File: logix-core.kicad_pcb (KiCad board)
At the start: 6 copper layers, 82 parts, among them J1 QSH-030-01-X-D-A-XX, J2 QSH-030-01-X-D-A-XX, J3 878321420, U1 XC7A15T-CSG325, U2 MP5470GL-0000-P, U3 TPUSBLC6-4SC6, U4 FT230XQ, U5 MX25L3233FZN, U6 XC7A15T-CSG325, U8 MT41K256M16TW-107:P

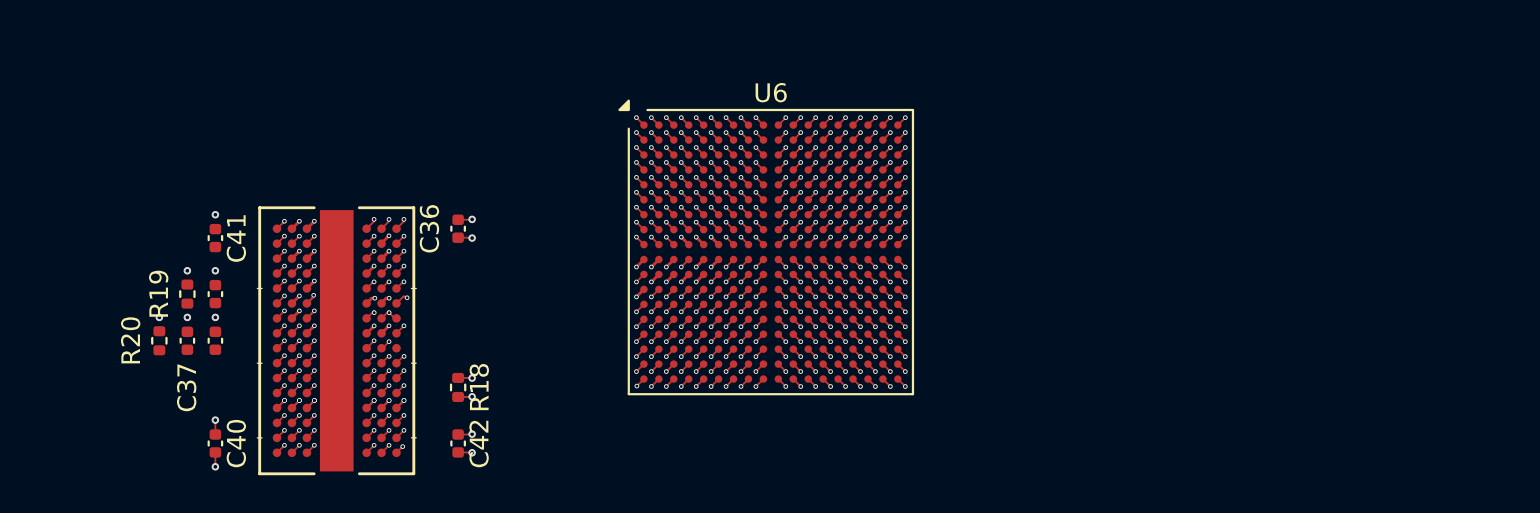
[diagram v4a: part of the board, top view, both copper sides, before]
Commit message: changed die to pad length for ddr3
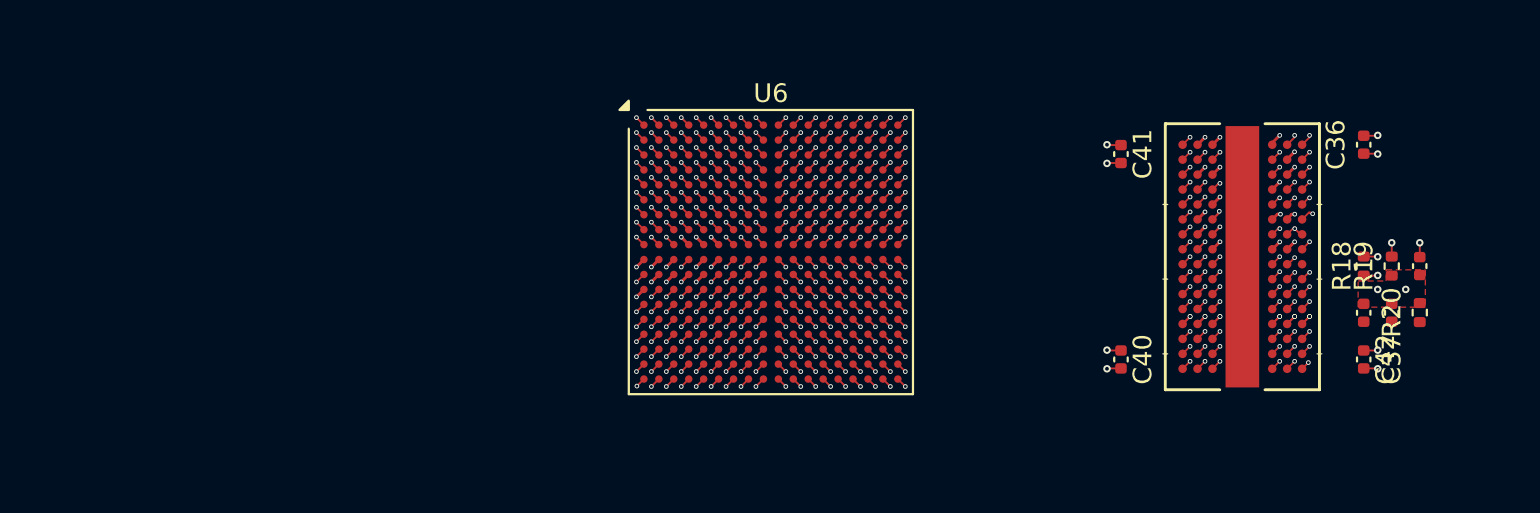
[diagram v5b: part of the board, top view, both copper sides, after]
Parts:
- moved R20 67.5 mm to (216.0, 146.0)
- moved C37 64.5 mm to (214.5, 146.0)
- moved C39 64.5 mm to (216.0, 143.5)
- moved R19 64.5 mm to (214.5, 143.5)
- moved C38 61.5 mm to (213.0, 146.0)
- moved R18 48.9 mm to (213.0, 143.5), turned to 90 degrees
- moved C36 48.7 mm to (213.0, 137.0)
- moved C40 48.7 mm to (200.0, 148.5)
- moved C41 48.7 mm to (200.0, 137.5)
- moved C42 48.7 mm to (213.0, 148.5)
- moved U8 48.7 mm to (206.5, 143.0)
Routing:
- net /DDR3_DQ10: track 1.13 -> 26.0 mm
- net /DDR3_DQ9: track 9.31 -> 25.3 mm
- net /DDR3_DQ8: track 16.5 -> 31.1 mm
- net /DDR3_UDQS-: track 14.2 -> 1.13 mm
- net /DDR3_UDQS+: track 14.2 -> 1.13 mm
- net /DDR3_DQ14: track 21.3 -> 33.5 mm
- net /DDR3_DQ11: track 23.0 -> 25.8 mm
- net /DDR3_DQ12: track 20.3 -> 22.7 mm
- net +1V5: track 13.7 -> 16.0 mm, vias 23 -> 26
- net /DDR3_DQ13: track 25.9 -> 24.2 mm
- net GND: track 57.5 -> 58.2 mm, vias 99 -> 100
- net /DDR3_DQ5: track 1.70 -> 2.27 mm
- net /DDR3_DQ15: track 23.2 -> 23.7 mm
- net /DDR3/DDR_VREF: vias 2 -> 4
- net (no net): vias 218 -> 212
- added copper zone on F.Cu, net /DDR3/DDR_VREF

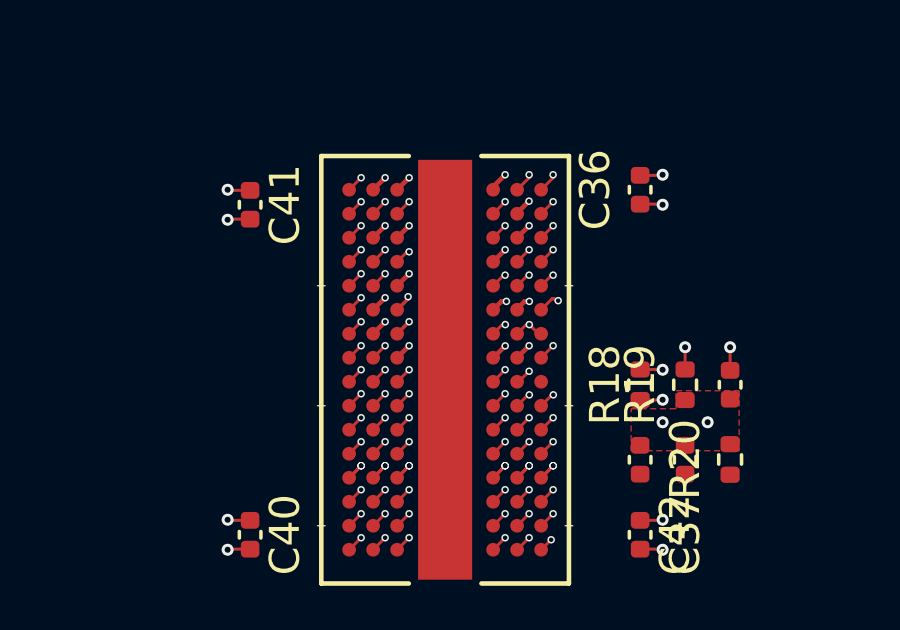
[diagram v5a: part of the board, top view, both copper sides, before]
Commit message: did preliminary routing on ddr3, fixed clearance rule
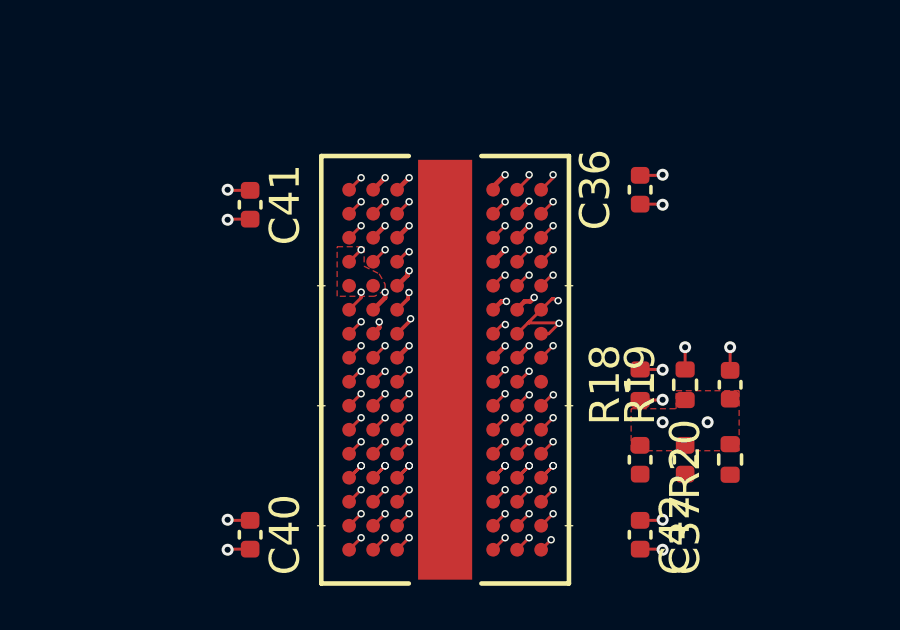
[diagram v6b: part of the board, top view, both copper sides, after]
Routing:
- net /DDR3_DQ5: track 2.27 -> 46.9 mm
- net /DDR3_DQ1: track 1.12 -> 36.1 mm
- net /DDR3_DQ4: track 1.70 -> 34.8 mm
- net /DDR3_DQ0: track 1.70 -> 34.4 mm
- net /DDR3_DQ3: track 1.11 -> 32.5 mm
- net /DDR3_DQ7: track 1.14 -> 32.4 mm
- net /DDR3_LDQS+: track 1.15 -> 31.5 mm
- net /DDR3_UDQS+: track 1.13 -> 30.8 mm
- net /DDR3_LDQS-: track 1.13 -> 30.6 mm
- net /DDR3_DQ6: track 1.13 -> 30.3 mm
- net /DDR3_UDQS-: track 1.13 -> 30.1 mm
- net /DDR3_DQ2: track 1.13 -> 29.6 mm
- net /DDR3_DQ10: track 26.0 -> 30.0 mm
- net /DDR3_DQ9: track 25.3 -> 29.1 mm
- net /DDR3_DQ12: track 22.7 -> 26.0 mm
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- added copper zone on F.Cu, net GND

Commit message: placed decoupling caps for fpga
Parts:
- removed U1 (x2): XC7A15T-CSG325, Package_BGA:Xilinx_CSG325
- added C43: 47u, Capacitor_SMD:C_1210_3225Metric, F.Cu at (193.0, 153.5)
- added C44: 4.7u, Capacitor_SMD:C_0402_1005Metric, F.Cu at (191.5, 148.5)
- added C45: 4.7u, Capacitor_SMD:C_0402_1005Metric, F.Cu at (186.0, 153.0)
- added C46: 0.47u, Capacitor_SMD:C_0402_1005Metric, F.Cu at (191.5, 147.0)
- added C47: 0.47u, Capacitor_SMD:C_0402_1005Metric, F.Cu at (191.5, 150.0)
- added C48: 0.47u, Capacitor_SMD:C_0402_1005Metric, F.Cu at (183.0, 153.0)
- added C49: 4.7u, Capacitor_SMD:C_0402_1005Metric, F.Cu at (186.8, 132.5)
- added C50: 4.7u, Capacitor_SMD:C_0402_1005Metric, F.Cu at (191.5, 136.5)
- added C51: 0.47u, Capacitor_SMD:C_0402_1005Metric, F.Cu at (185.0, 132.5)
- added C52: 0.47u, Capacitor_SMD:C_0402_1005Metric, F.Cu at (188.5, 132.5)
- added C53: 0.47u, Capacitor_SMD:C_0402_1005Metric, F.Cu at (191.5, 139.5)
- added C54: 47u, Capacitor_SMD:C_1210_3225Metric, F.Cu at (169.5, 153.5)
- added C55: 4.7u, Capacitor_SMD:C_0402_1005Metric, F.Cu at (177.0, 153.0)
- added C56: 4.7u, Capacitor_SMD:C_0402_1005Metric, F.Cu at (171.0, 146.5)
- added C57: 0.47u, Capacitor_SMD:C_0402_1005Metric, F.Cu at (171.0, 149.5)
- added C58: 0.47u, Capacitor_SMD:C_0402_1005Metric, F.Cu at (178.5, 153.0)
- added C59: 0.47u, Capacitor_SMD:C_0402_1005Metric, F.Cu at (171.0, 143.5)
- added C60: 0.47u, Capacitor_SMD:C_0402_1005Metric, F.Cu at (180.0, 153.0)
- added C61: 0.47u, Capacitor_SMD:C_0402_1005Metric, F.Cu at (191.5, 135.0)
- added C62: 0.47u, Capacitor_SMD:C_0402_1005Metric, F.Cu at (174.0, 153.0)
- added C63: 47u, Capacitor_SMD:C_1210_3225Metric, F.Cu at (193.0, 132.0)
- C1, C12, C13, C14, C15, C2, C3, C31, C32, C33, C34, C8: footprint Capacitor_SMD:C_0603_1608Metric -> Capacitor_SMD:C_0402_1005Metric
- C10, C11, C30, C35, C4, C5: footprint Capacitor_SMD:C_0805_2012Metric -> Capacitor_SMD:C_0402_1005Metric
- moved C10 223.1 mm to (182.0, 132.5), turned to 90 degrees
- moved R17 219.7 mm to (213.0, 60.8)
- moved C29 212.2 mm to (208.0, 53.8)
- moved C1 75.2 mm to (191.5, 144.0)
- moved C4 73.8 mm to (191.5, 145.5)
- moved C5 67.9 mm to (191.5, 142.5)
- moved C3 67.7 mm to (191.5, 141.0)
- moved R12 67.3 mm to (152.8, 156.3)
- moved R15 67.3 mm to (152.8, 162.2)
- moved R11 67.3 mm to (152.8, 154.3)
- moved R13 67.3 mm to (152.8, 158.3)
- moved R14 67.3 mm to (152.8, 160.2)
- moved R16 67.3 mm to (158.0, 154.3)
- moved C2 67.3 mm to (191.5, 138.0)
- moved C7 54.0 mm to (169.5, 132.0), turned to 180 degrees
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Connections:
- C10 pad 1: +V1P0 -> /FPGA/FPGA pg.4/VCCINT
- C11 pad 1: +V1P0 -> /FPGA/FPGA pg.4/VCCINT
- C12 pad 1: +V1P0 -> /FPGA/FPGA pg.4/VCCINT
- C13 pad 1: +V1P0 -> /FPGA/FPGA pg.4/VCCINT
- C9 pad 1: +V1P0 -> /FPGA/FPGA pg.4/VCCINT
- R17 pad 2: Net-(U1D-MGTRREF_216) -> Net-(U6D-MGTRREF_216) (x2)
- U6 pad A16: unconnected-(U6A-VCCO_15-PadA16) -> /FPGA/FPGA pg.1/VCCO15
- U6 pad A2: (no net) -> +V1P2
- U6 pad A6: (no net) -> Net-(U6D-MGTRREF_216)
- U6 pad B13: unconnected-(U6A-VCCO_15-PadB13) -> /FPGA/FPGA pg.1/VCCO15
- U6 pad B4: (no net) -> +V1P0
- U6 pad C1: (no net) -> +V1P2
- U6 pad C10: unconnected-(U6A-VCCO_15-PadC10) -> /FPGA/FPGA pg.1/VCCO15
- U6 pad C5: (no net) -> +V1P0
- U6 pad D17: unconnected-(U6A-VCCO_15-PadD17) -> /FPGA/FPGA pg.1/VCCO15
- U6 pad E1: (no net) -> +V1P2
- U6 pad E10: unconnected-(U6E-VCCO_0-PadE10) -> /FPGA/FPGA pg.3/VCCO_0
- U6 pad E14: unconnected-(U6A-VCCO_15-PadE14) -> /FPGA/FPGA pg.1/VCCO15
- U6 pad E5: (no net) -> +V1P0
- U6 pad F3: (no net) -> +V1P2
- U6 pad F5: (no net) -> +V1P0
- U6 pad F7: +V1P0 -> /FPGA/FPGA pg.4/VCCINT
- U6 pad F9: +V1P0 -> /FPGA/FPGA pg.4/VCCINT
- U6 pad G18: unconnected-(U6A-VCCO_15-PadG18) -> /FPGA/FPGA pg.1/VCCO15
- U6 pad G2: (no net) -> +V1P2
- U6 pad G8: +V1P0 -> /FPGA/FPGA pg.4/VCCINT
- U6 pad H15: unconnected-(U6A-VCCO_15-PadH15) -> /FPGA/FPGA pg.1/VCCO15
- U6 pad H7: +V1P0 -> /FPGA/FPGA pg.4/VCCINT
- U6 pad H9: +V1P0 -> /FPGA/FPGA pg.4/VCCINT
- U6 pad J12: +V1P0 -> /FPGA/FPGA pg.4/VCCINT
- U6 pad J8: +V1P0 -> /FPGA/FPGA pg.4/VCCINT
- U6 pad K11: +V1P0 -> /FPGA/FPGA pg.4/VCCINT
- U6 pad K7: +V1P0 -> /FPGA/FPGA pg.4/VCCINT
- U6 pad L12: +V1P0 -> /FPGA/FPGA pg.4/VCCINT
- U6 pad L16: unconnected-(U6A-VCCO_14-PadL16) -> /FPGA/FPGA pg.1/VCCO14
- U6 pad L6: unconnected-(U6B-VCCO_34-PadL6) -> /FPGA/FPGA pg.2/VCCO34
- U6 pad L8: +V1P0 -> /FPGA/FPGA pg.4/VCCINT
- U6 pad M11: +V1P0 -> /FPGA/FPGA pg.4/VCCINT
- U6 pad M3: unconnected-(U6B-VCCO_34-PadM3) -> /FPGA/FPGA pg.2/VCCO34
- U6 pad M7: +V1P0 -> /FPGA/FPGA pg.4/VCCINT
- U6 pad N10: +V1P0 -> /FPGA/FPGA pg.4/VCCINT
- U6 pad N12: +V1P0 -> /FPGA/FPGA pg.4/VCCINT
- U6 pad N8: +V1P0 -> /FPGA/FPGA pg.4/VCCINT
- U6 pad P11: +V1P0 -> /FPGA/FPGA pg.4/VCCINT
- U6 pad P17: unconnected-(U6A-VCCO_14-PadP17) -> /FPGA/FPGA pg.1/VCCO14
- U6 pad P7: unconnected-(U6B-VCCO_34-PadP7) -> /FPGA/FPGA pg.2/VCCO34
- U6 pad P9: +V1P0 -> /FPGA/FPGA pg.4/VCCINT
- U6 pad R10: unconnected-(U6E-VCCO_0-PadR10) -> /FPGA/FPGA pg.3/VCCO_0
- U6 pad R14: unconnected-(U6A-VCCO_14-PadR14) -> /FPGA/FPGA pg.1/VCCO14
- U6 pad R4: unconnected-(U6B-VCCO_34-PadR4) -> /FPGA/FPGA pg.2/VCCO34
- U6 pad T1: unconnected-(U6B-VCCO_34-PadT1) -> /FPGA/FPGA pg.2/VCCO34
- U6 pad T11: unconnected-(U6A-VCCO_14-PadT11) -> /FPGA/FPGA pg.1/VCCO14
- U6 pad U18: unconnected-(U6A-VCCO_14-PadU18) -> /FPGA/FPGA pg.1/VCCO14
- U6 pad U8: unconnected-(U6A-VCCO_14-PadU8) -> /FPGA/FPGA pg.1/VCCO14
- U6 pad V15: unconnected-(U6A-VCCO_14-PadV15) -> /FPGA/FPGA pg.1/VCCO14
- U6 pad V5: unconnected-(U6B-VCCO_34-PadV5) -> /FPGA/FPGA pg.2/VCCO34
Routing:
- net (no net): track 148.5 -> 0.00 mm, vias 212 -> 0
- net +V1P2: track 23.3 -> 2.83 mm, vias 33 -> 8
- net /FPGA/FPGA pg.4/VCCINT: track 0.00 -> 10.2 mm, vias 0 -> 21
- net +V1P0: track 13.3 -> 3.96 mm, vias 23 -> 12
- net /FPGA/FPGA pg.1/VCCO14: track 0.00 -> 7.75 mm, vias 0 -> 15
- net /FPGA/FPGA pg.1/VCCO15: track 0.00 -> 7.75 mm, vias 0 -> 12
- net GND: track 58.8 -> 66.5 mm, vias 98 -> 114
- net /DDR3_DQ12: track 26.0 -> 21.0 mm
- net /DDR3_DQ9: track 29.1 -> 24.1 mm
- net /DDR3_UDQS+: track 30.8 -> 25.8 mm
- net /DDR3_LDQS-: track 30.6 -> 25.6 mm
- net /DDR3_LDQS+: track 31.5 -> 26.5 mm
- net /DDR3_DQ8: track 31.1 -> 26.1 mm
- net /DDR3_DQ7: track 32.4 -> 27.4 mm
- net /DDR3_DQ6: track 30.3 -> 25.3 mm
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- added copper zone on F.Cu, net +V1P0
- added copper zone on In4.Cu, net +V1P0
- added copper zone on F.Cu, net +V1P2
- added copper zone on In4.Cu, net +V1P2
- added copper zone on F.Cu, net /FPGA/FPGA pg.1/VCCO14
- added copper zone on In4.Cu, net /FPGA/FPGA pg.1/VCCO14
- added copper zone on F.Cu, net /FPGA/FPGA pg.2/VCCO34
- added copper zone on F.Cu, net /FPGA/FPGA pg.4/VCCINT
- added copper zone on In4.Cu, net /FPGA/FPGA pg.4/VCCINT

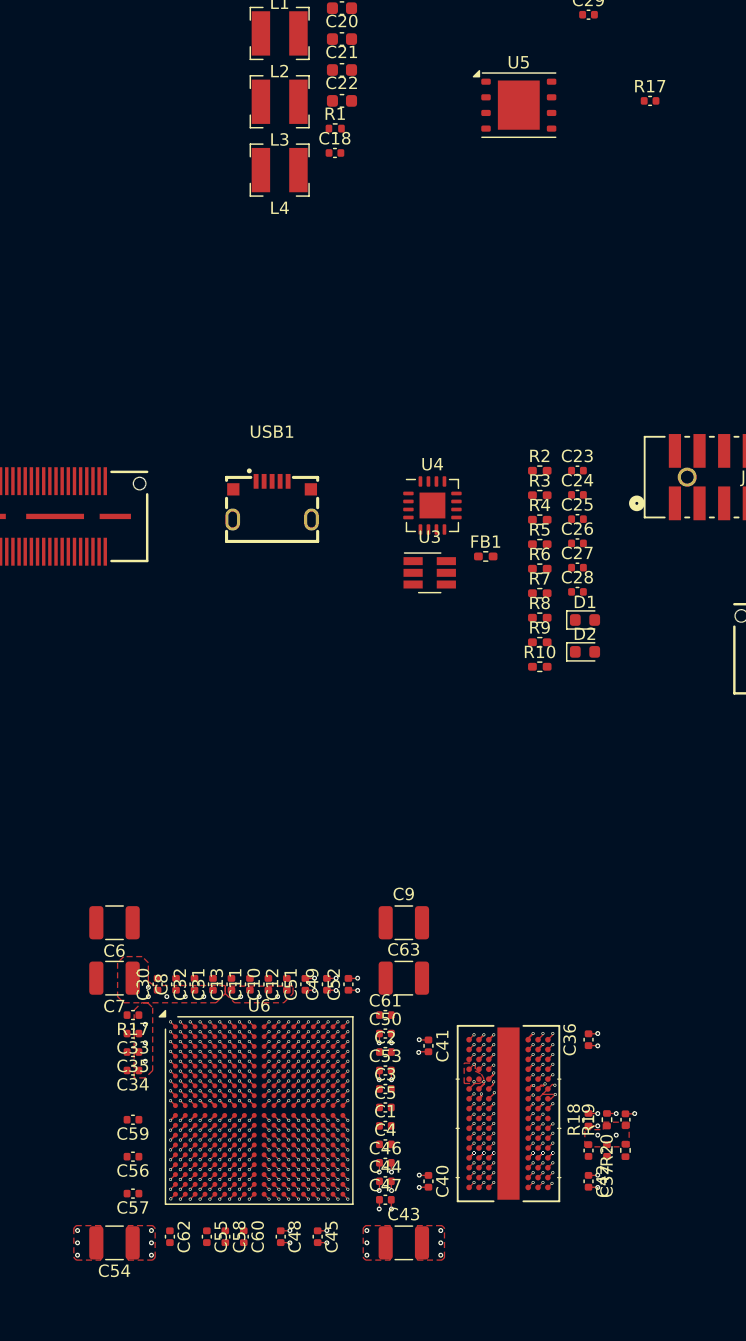
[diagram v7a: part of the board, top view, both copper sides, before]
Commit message: more power-work, vccint needs to be moved to left side still
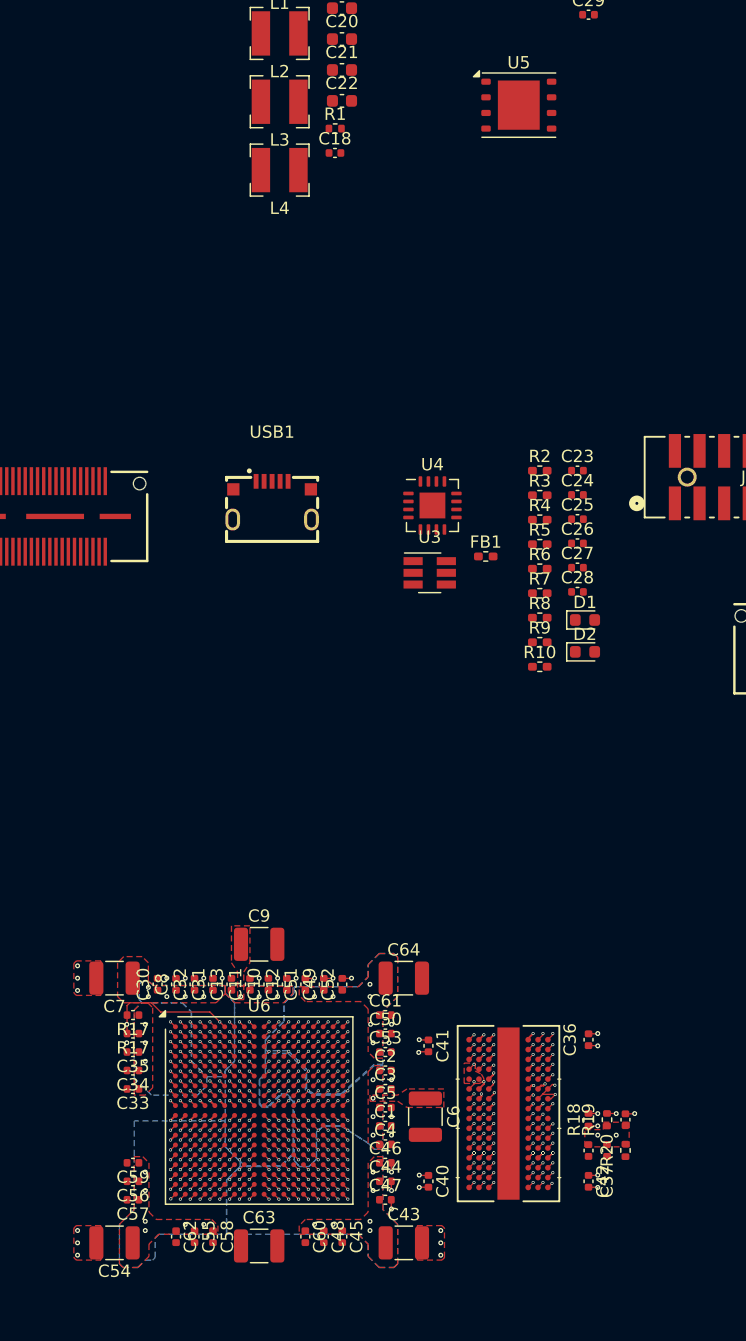
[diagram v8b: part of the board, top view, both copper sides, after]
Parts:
- added C64: 47u, Capacitor_SMD:C_1210_3225Metric, F.Cu at (193.0, 132.0)
- moved R17 86.6 mm to (171.0, 136.5), turned to 180 degrees
- moved C6 29.8 mm to (194.8, 143.2), turned to -90 degrees
- moved C63 24.7 mm to (181.2, 153.8)
- moved C9 11.9 mm to (181.2, 129.2)
- moved C60 5.00 mm to (185.0, 153.0)
- moved C33 4.50 mm to (171.0, 141.0)
- moved C48 3.50 mm to (186.5, 153.0)
- moved C59 3.50 mm to (171.0, 147.0)
- moved C45 2.00 mm to (188.0, 153.0)
- moved C56 2.00 mm to (171.0, 148.5)
- moved C2 1.50 mm to (191.5, 139.5)
- moved C53 1.50 mm to (191.5, 138.0)
- moved C55 1.00 mm to (176.0, 153.0)
- moved C58 1.00 mm to (177.5, 153.0)
- moved C52 0.50 mm to (188.0, 132.5)
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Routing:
- net Net-(U6D-MGTRREF_216): track 0.57 -> 11.1 mm
- net /FPGA/FPGA pg.1/VCCO14: track 7.75 -> 3.96 mm, vias 15 -> 13
- net /FPGA/FPGA pg.1/VCCO15: track 7.75 -> 3.96 mm, vias 12 -> 13
- net GND: track 66.5 -> 63.4 mm, vias 114 -> 127
- net /DDR3_DQ1: track 31.1 -> 32.2 mm
- net /DDR3_DQ0: track 29.4 -> 30.2 mm
- net /DDR3_DQ5: track 41.9 -> 42.4 mm
- net /FPGA/FPGA pg.2/VCCO34: vias 9 -> 12
- net +V1P8: vias 7 -> 11
- added copper zone on B.Cu, net +V1P0
- added copper zone on B.Cu, net +V1P2
- added copper zone on B.Cu, net +V1P8
- added copper zone on F.Cu, net +V1P8
- added copper zone on B.Cu, net /FPGA/FPGA pg.1/VCCO14
- added copper zone on B.Cu, net /FPGA/FPGA pg.1/VCCO15
- added copper zone on F.Cu, net /FPGA/FPGA pg.1/VCCO15
- added copper zone on B.Cu, net /FPGA/FPGA pg.2/VCCO34
- added copper zone on B.Cu, net /FPGA/FPGA pg.4/VCCINT
- removed copper zone on In4.Cu, net +V1P0
- removed copper zone on In4.Cu, net +V1P2
- removed copper zone on In4.Cu, net /FPGA/FPGA pg.1/VCCO14
- removed copper zone on In4.Cu, net /FPGA/FPGA pg.4/VCCINT
